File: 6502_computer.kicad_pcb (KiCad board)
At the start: 4 copper layers, 169.5 x 112.1 mm, 19 parts, among them J1 Barrel_Jack_Switch, J2 Conn_01x16, J3 Mega, J4 Mega, J5 Clock, J6 Conn_01x40, J7 Conn_01x06, J8 Conn_01x02, J9 Conn_01x02, U1 6502_mainboard_v2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

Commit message: Update
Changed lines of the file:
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@@
     (fp_line (start 68 3) (end 68 28) (layer "F.SilkS") (width 0.12))
     (fp_arc (start -0.29972 8.49884) (mid -0.153162 8.145018) (end 0.20066 7.99846) (layer "F.SilkS") (width 0.12))
-    (fp_arc (start 64.20104 22.49932) (mid 64.054479 22.85315) (end 63.70066 22.9997) (layer "F.SilkS") (width 0.12))
+    (fp_arc (start 64.20104 22.49932) (mid 64.054473 22.853115) (end 63.70066 22.9997) (layer "F.SilkS") (width 0.12))
     (fp_arc (start 0.20066 22.9997) (mid -0.153162 22.853142) (end -0.29972 22.49932) (layer "F.SilkS") (width 0.12))
     (fp_arc (start 63.7 8) (mid 64.053553 8.146447) (end 64.2 8.5) (layer "F.SilkS") (width 0.12))

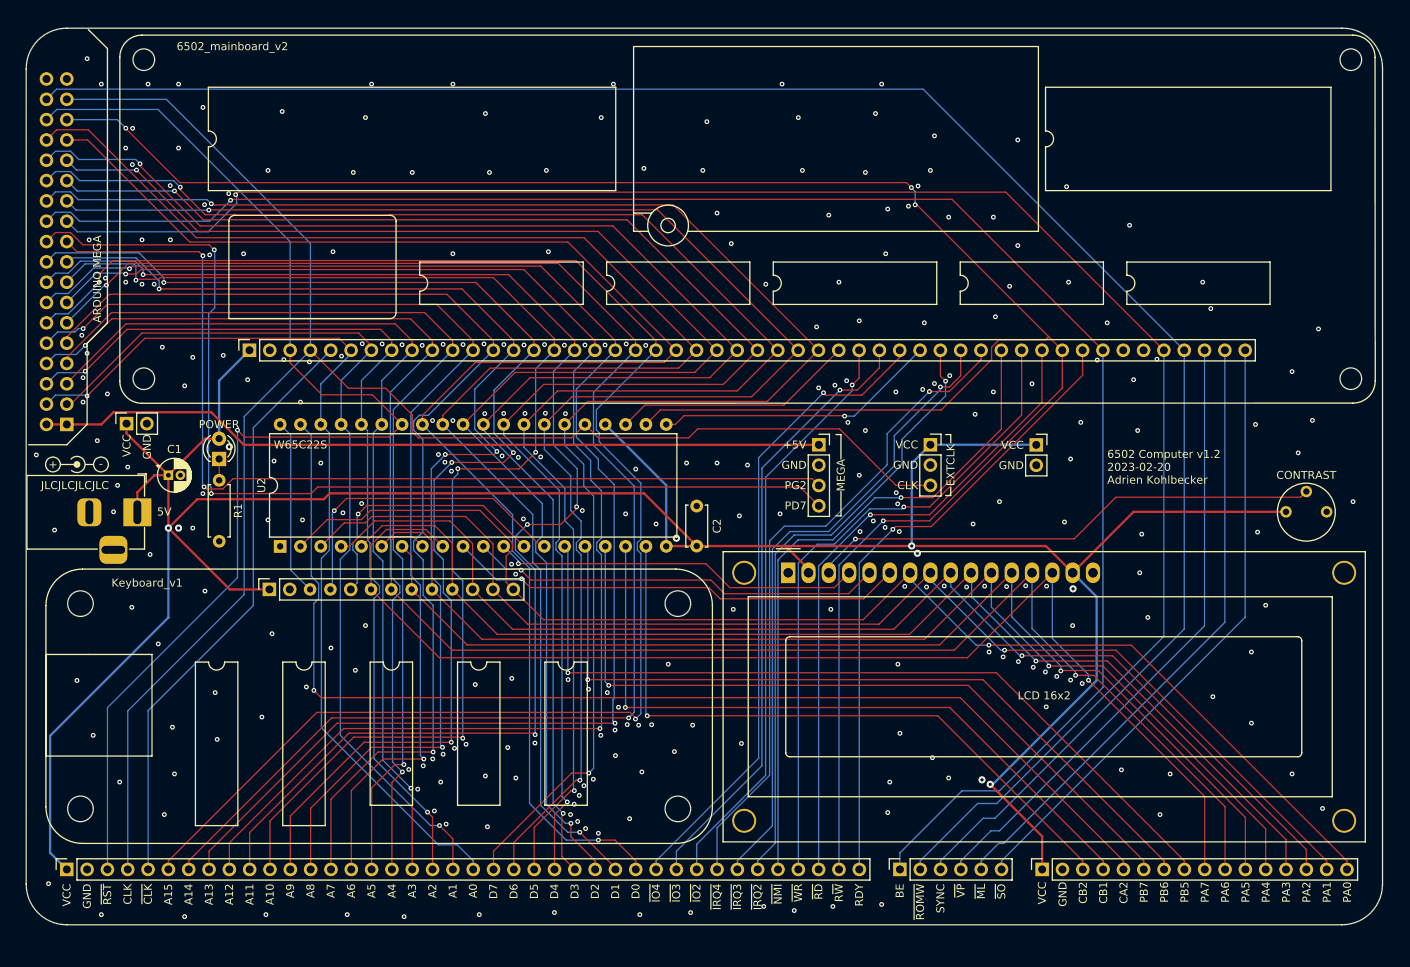
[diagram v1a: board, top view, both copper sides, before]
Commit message: Move to two layers
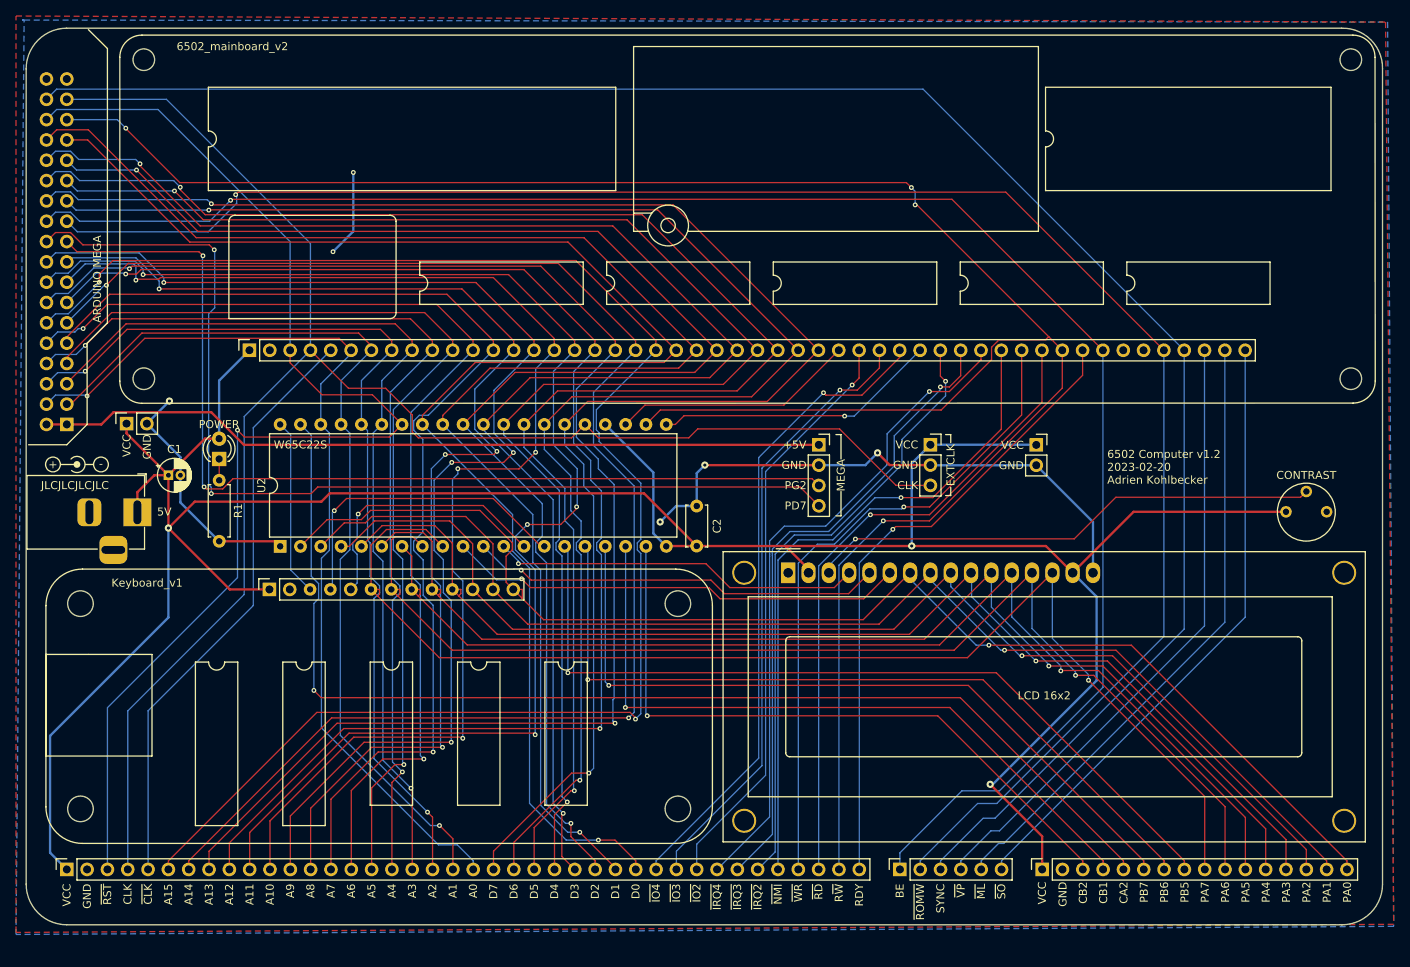
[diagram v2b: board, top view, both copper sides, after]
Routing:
- net GND: track 0.00 -> 111.3 mm, vias 291 -> 6
- net /PA0: track 161.2 -> 163.5 mm
- net /PA5: track 139.5 -> 141.5 mm
- net /PA4: track 144.7 -> 146.7 mm
- net /PA7: track 154.3 -> 156.3 mm
- net /PA6: track 146.4 -> 148.4 mm
- net /PA3: track 148.1 -> 150.1 mm
- net /PA2: track 151.7 -> 152.8 mm
- net /PA1: track 155.4 -> 156.4 mm
- net /KB_E: track 33.5 -> 34.1 mm
- added copper zone on F.Cu, net GND
- added copper zone on B.Cu, net VCC
- removed copper zone on In1.Cu, net GND
- removed copper zone on In2.Cu, net GND
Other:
- copper layers 4 -> 2
